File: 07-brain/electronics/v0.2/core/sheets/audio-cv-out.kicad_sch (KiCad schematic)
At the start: 28 parts, among them U4 TL072, U5 TL072, U6 MCP4822, U7 74HC4053B

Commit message: Added output buffer to Brain
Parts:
- added C19, C20: 100n, Capacitor_SMD:C_0603_1608Metric, symbol Device:C
- added U11: TL072, Package_SO:SOIC-8_3.9x4.9mm_P1.27mm, symbol Amplifier_Operational:TL072
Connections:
- net +12V: now also C19.1, U11.8 (V+)
- net -12V: now also C20.2, U11.4 (V-)
- net AUDIO_CV_OUT_1: now also U11.6 (-)
- net AUDIO_CV_OUT_2: now also U11.2 (-)
- net GND: now also C19.2, C20.1
- net at R21.2, U5.7: now also U11.5 (+); no longer R23.1
- net at R20.2, U4.7: now also U11.3 (+); no longer R22.1
- new net: R22.1, U11.1
- new net: R23.1, U11.7
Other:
- moved on the sheet: R22, R23, U5C

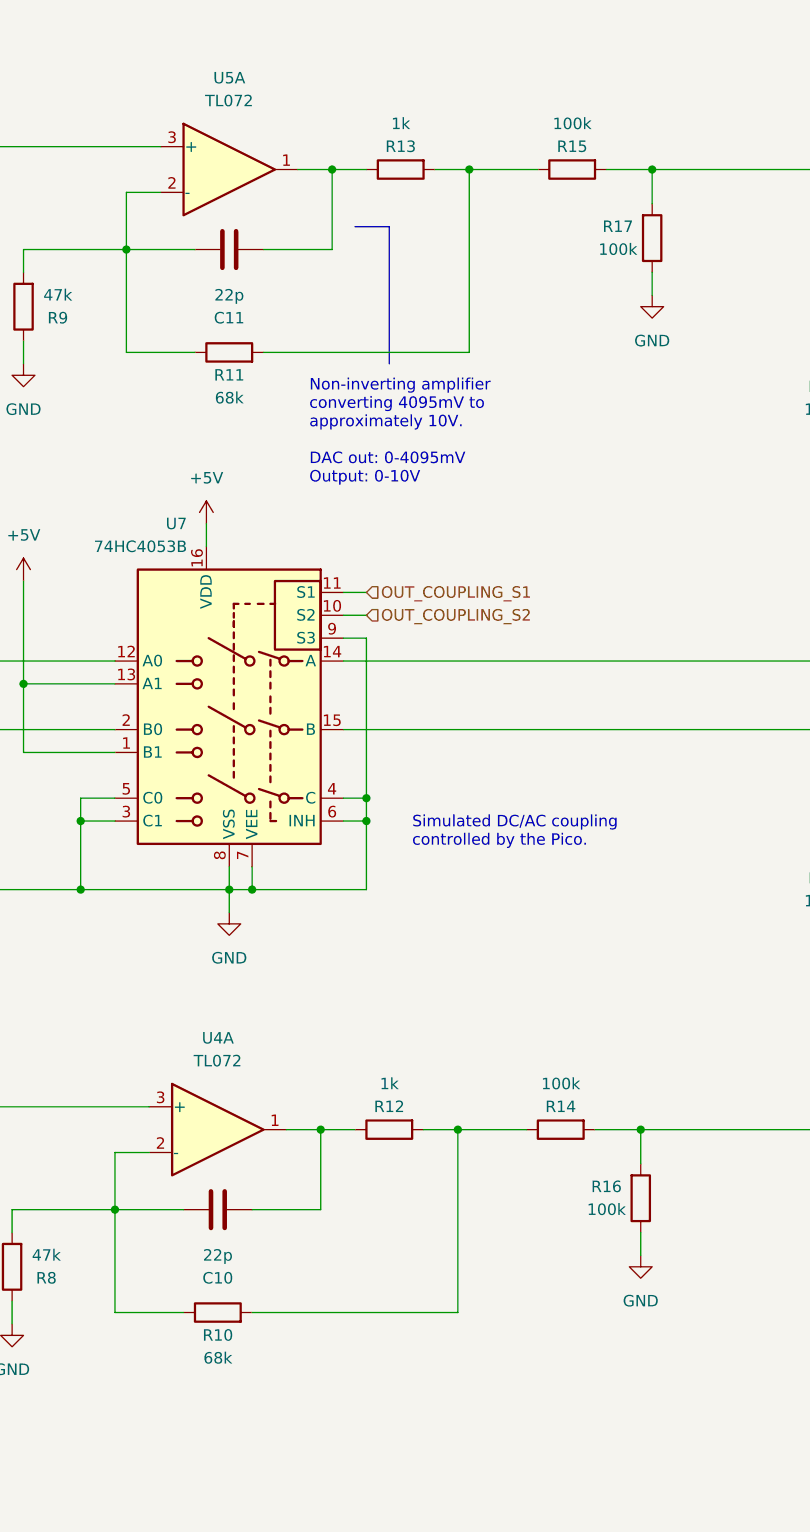
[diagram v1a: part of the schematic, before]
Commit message: Added CV gain trimmer to Brain
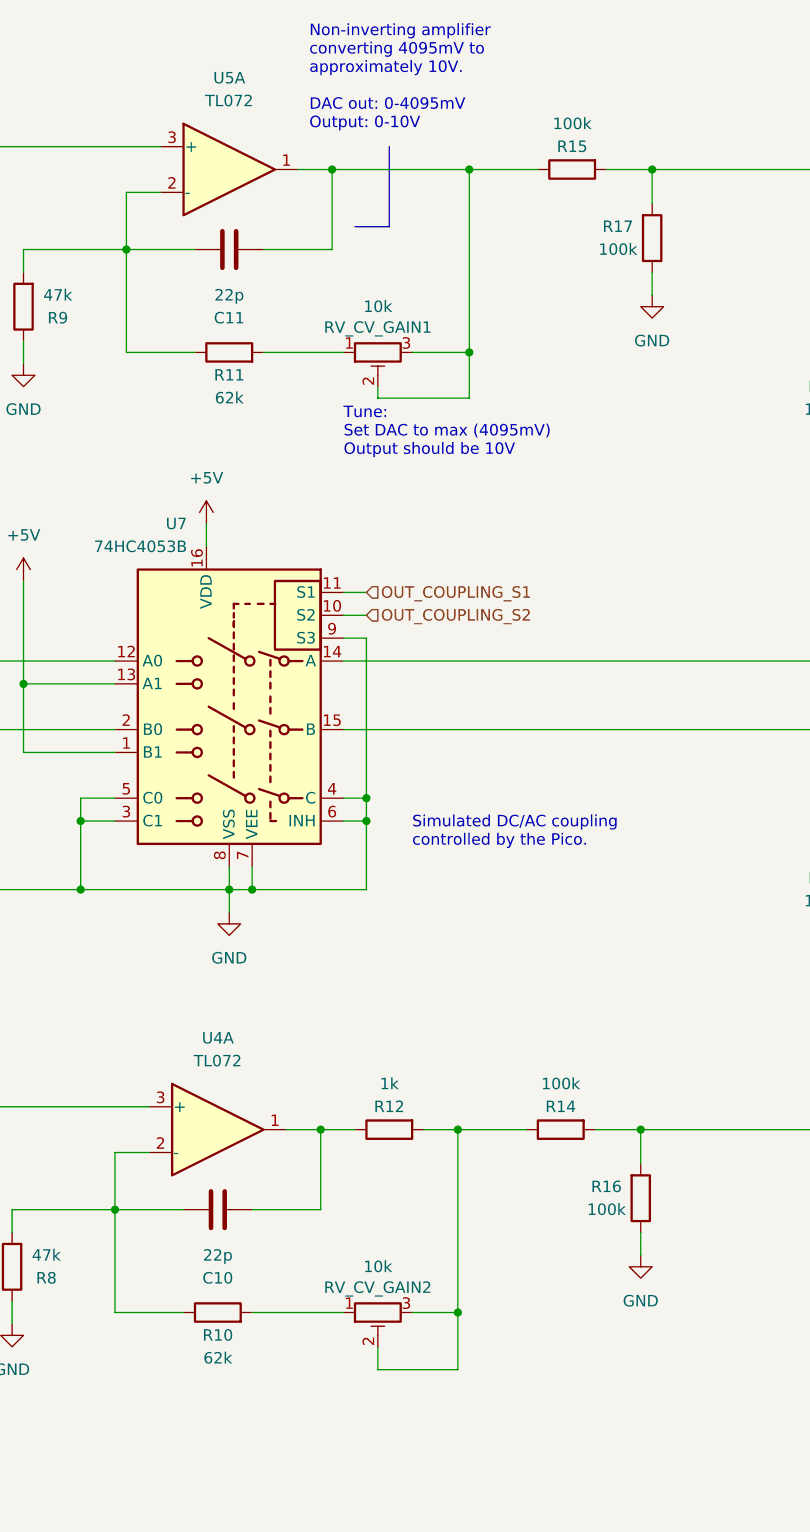
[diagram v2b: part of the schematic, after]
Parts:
- removed R13: 1k, Resistor_SMD:R_0603_1608Metric, symbol Device:R
- added RV_CV_GAIN1, RV_CV_GAIN2: 10k, Potentiometer_THT:Potentiometer_ACP_CA6-H2,5_Horizontal, symbol Device:R_Potentiometer_Trim
- R10, R11: value 68k -> 62k; LCSC C23231 -> C23221
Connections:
- net at R15.1: now also C11.2, U5.1, RV_CV_GAIN1.2, RV_CV_GAIN1.3; no longer R11.2
- net at R12.2, R14.1: now also RV_CV_GAIN2.2, RV_CV_GAIN2.3; no longer R10.2
- new net: R11.2, RV_CV_GAIN1.1
- new net: R10.2, RV_CV_GAIN2.1
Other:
- note added: "Tune: Set DAC to max (4095mV) Output should be 10V"
